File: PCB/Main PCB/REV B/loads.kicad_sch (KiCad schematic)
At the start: 27 parts, among them Q3 2N7002, Q4 2N7002, Q5 2N7002, U10 ALDP105W, U11 TLP2362TPR_E, U12 ALDP105W, U7 ALDP105W, U8 TLP2362TPR_E, U9 TLP2362TPR_E

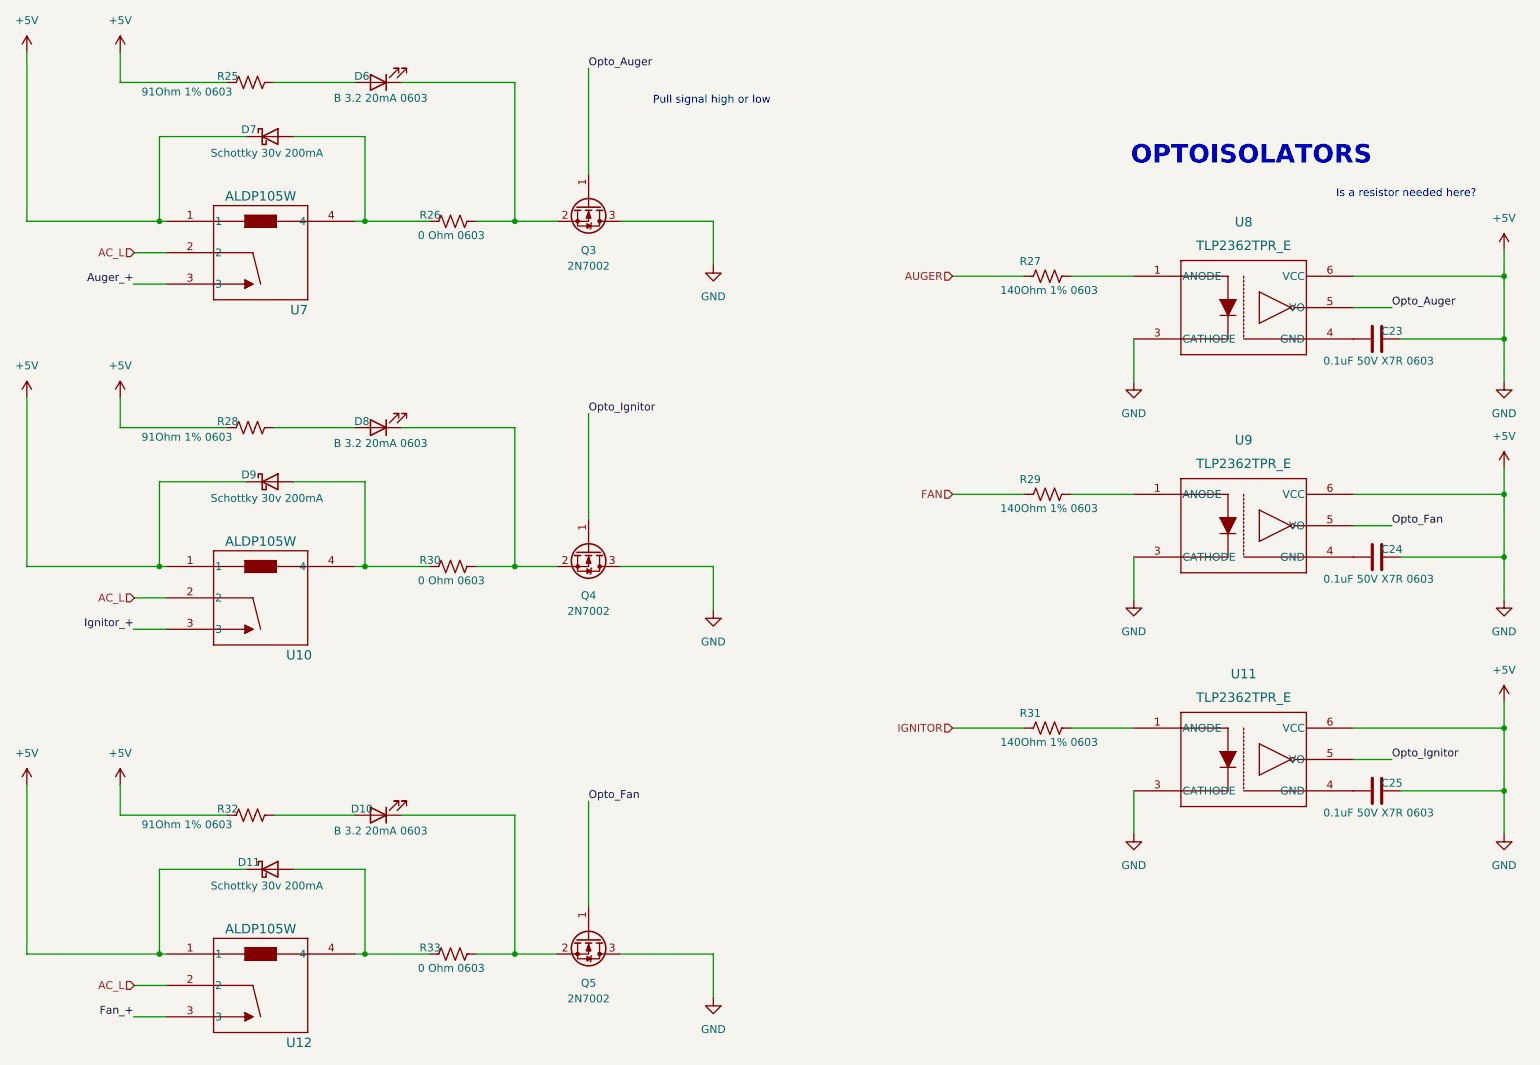
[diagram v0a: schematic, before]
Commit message: PCB schematic updates, Changed transistor on reboot to double
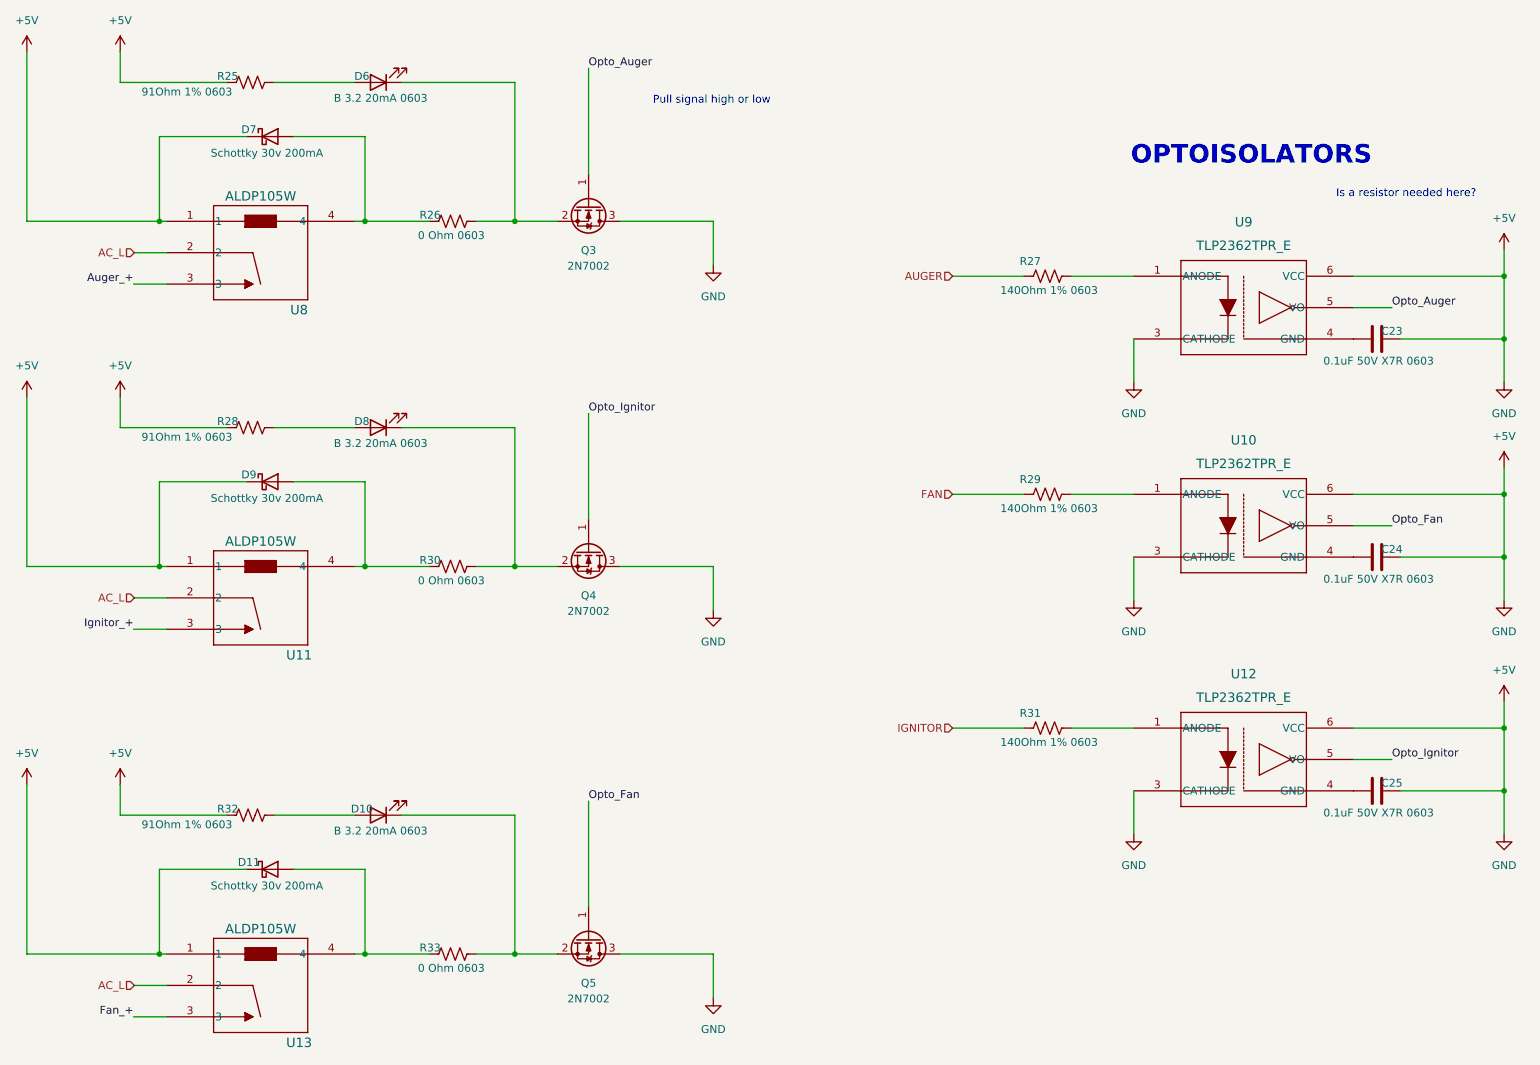
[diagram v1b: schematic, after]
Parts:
- renumbered U9 to U10, U10 to U11, U11 to U12, U12 to U13, U7 to U8, U8 to U9
